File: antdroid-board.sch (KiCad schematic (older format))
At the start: 7 parts

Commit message: Added Servo Power Supply
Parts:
- added C? (x2): 200µF, symbol C
- added C? (x2): 0.01µF, symbol C
- added C? (x2): 500µF, symbol C
- added D?: 1N5822, DO-204AL, symbol 1N5822
- added D?: MBR745, TO-220, symbol MBR745
- added IC?: LT1076CT, linear-technology-2-TO220-5, symbol LT1076CT
- added IC?: LT1074CT, linear-technology-2-TO220-5, symbol LT1074CT
- added L?: 100µH, symbol INDUCTOR
- added L?: 50µH, symbol INDUCTOR
- added R? (x2): 2.7k, symbol R
- added R? (x2): 2.8k, symbol R
- added R? (x2): 2.21k, symbol R
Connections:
- net labels added: GND, VCC
- wire segments 16 -> 42
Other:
- note added: "RPI POWER SUPPLY"
- note added: "SERIAL RPI"
- note added: "SERVOS POWER SUPPLY"
- note removed: "SERIAL_RPI"
- moved on the sheet: SHIELD?

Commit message: Change power supply to LM26XX
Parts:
- removed C? (x2): 200µF, symbol C
- removed C? (x2): 0.01µF, symbol C
- removed C? (x2): 500µF, symbol C
- removed D?: 1N5822, DO-204AL, symbol 1N5822
- removed D?: MBR745, TO-220, symbol MBR745
- removed IC?: LT1076CT, linear-technology-2-TO220-5, symbol LT1076CT
- removed IC?: LT1074CT, linear-technology-2-TO220-5, symbol LT1074CT
- removed L?: 100µH, symbol INDUCTOR
- removed L?: 50µH, symbol INDUCTOR
- removed R? (x2): 10K, symbol R
- removed R? (x2): 2.7k, symbol R
- removed R? (x2): 2.8k, symbol R
- removed R? (x2): 2.21k, symbol R
- added C? (x6): 15µF/50V, symbol CP
- added C? (x2): 0,01µF, symbol C
- added C? (x2): 0.47µF, symbol C
- added C? (x4): 180µF/16V, symbol CP
- added C?: C, symbol C
- added C?: 10nF, symbol C
- added C?: 68µF, symbol C
- added D? (x2): MBR745G, DO-204AL, symbol MBR745G
- added D?: 1N5822, DO-204AL, symbol 1N5822
- added L? (x2): 22µH, symbol INDUCTOR
- added L?: 47µH, symbol INDUCTOR
- added R? (x2): 10K, symbol R
- added U? (x2): LM2678T-5.0, TO-220, symbol LM2678T-5.0
- added U?: LM2675M-5, SOIC-8, symbol LM2675M-5
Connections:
- net labels added: +5VA
- wire segments 42 -> 54
- no-connect marks 0 -> 1
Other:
- note added: "SERVO POWER LED"
- moved on the sheet: Q?, R?, SHIELD?

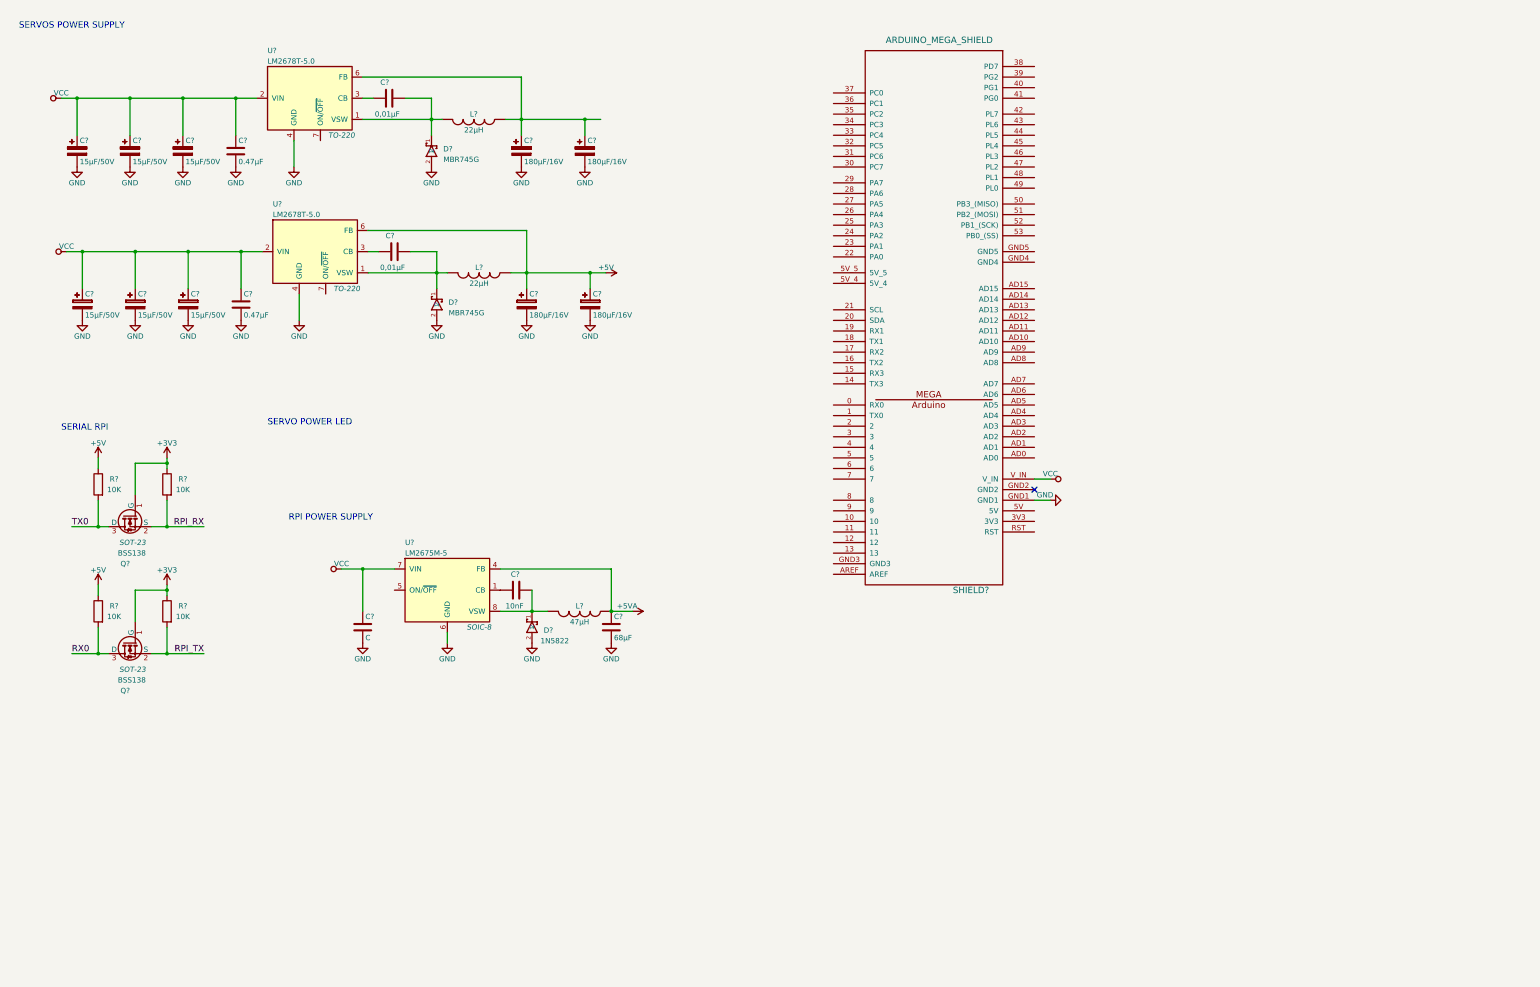
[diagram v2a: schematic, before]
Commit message: Added JP of servos
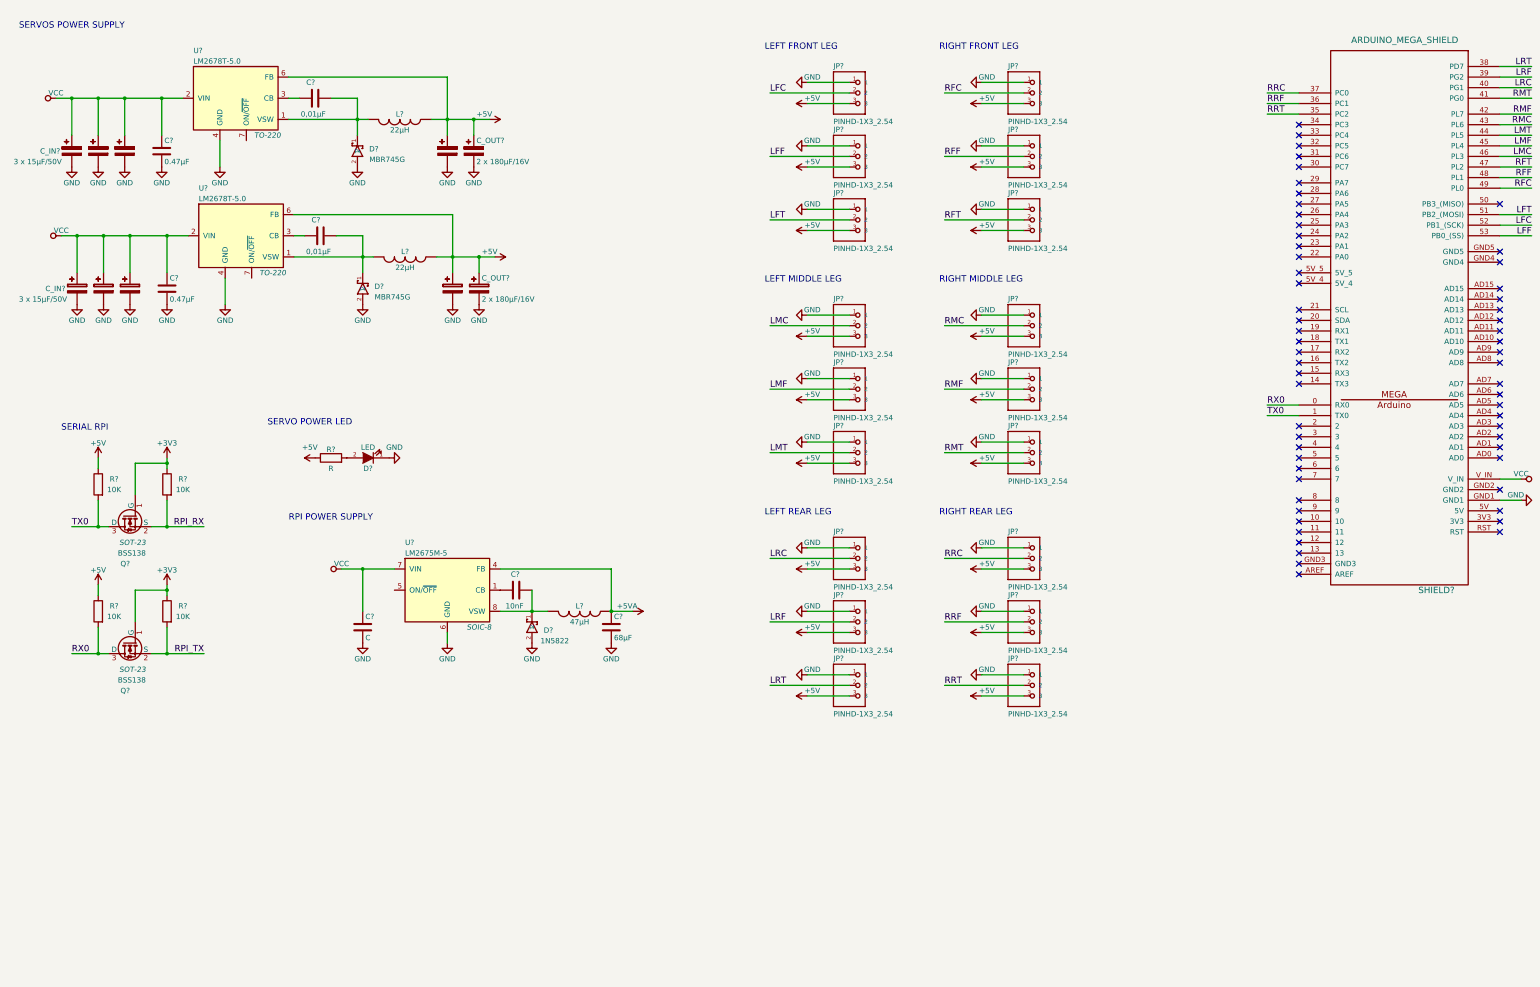
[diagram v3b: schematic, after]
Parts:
- removed C? (x3): 15µF/50V, symbol CP
- removed C?: 0.47µF, symbol C
- removed C?: 0,01µF, symbol C
- removed C? (x2): 180µF/16V, symbol CP
- removed D?: MBR745G, DO-204AL, symbol MBR745G
- removed L?: 22µH, symbol INDUCTOR
- removed U?: LM2678T-5.0, TO-220, symbol LM2678T-5.0
- added C? (x2): 15µF/50V, symbol CP
- added C?: 0.47µF, symbol C
- added C?: 0,01µF, symbol C
- added C?: 180µF/16V, symbol CP
- added C_IN?: 3 x 15µF/50V, symbol CP
- added C_OUT?: 2 x 180µF/16V, symbol CP
- added D?: MBR745G, DO-204AL, symbol MBR745G
- added D?: LED, symbol LED
- added JP? (x18): PINHD-1X3_2.54, pinhead-1-1X03, symbol PINHD-1X3_2.54
- added L?: 22µH, symbol INDUCTOR
- added R?: R, symbol R
- added U?: LM2678T-5.0, TO-220, symbol LM2678T-5.0
- C_IN?: renamed from C?; value 15µF/50V -> 3 x 15µF/50V
- C_OUT?: renamed from C?; value 180µF/16V -> 2 x 180µF/16V
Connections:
- net +5V: now also C?.1, C_OUT?.1, L?.1, U?.6 (FB), C?.1, C_OUT?.1, JP?.3, JP?.3, JP?.3, JP?.3, JP?.3, JP?.3, JP?.3, JP?.3, JP?.3, JP?.3, JP?.3, JP?.3, JP?.3, JP?.3, JP?.3, JP?.3, JP?.3, JP?.3, L?.1, R?.1, U?.6 (FB)
- net GND: now also C?.2, C?.2, C?.2, C?.2, C_IN?.2, C_OUT?.2, D?.1 (K), D?.2, JP?.1, JP?.1, JP?.1, JP?.1, JP?.1, JP?.1, JP?.1, JP?.1, JP?.1, JP?.1, JP?.1, JP?.1, JP?.1, JP?.1, JP?.1, JP?.1, JP?.1, JP?.1, U?.4 (GND)
- net RX0: now also SHIELD?.0 (RX0)
- net TX0: now also SHIELD?.1 (TX0)
- net VCC: now also C?.1, C?.1, C?.1, C_IN?.1, U?.2 (VIN)
- net RRT: now reaches SHIELD?.35 (PC2)
- net RRT: now also JP?.2
- net RRF: now reaches SHIELD?.36 (PC1)
- net RRF: now also JP?.2
- net RRC: now reaches SHIELD?.37 (PC0)
- net RRC: now also JP?.2
- net LRT: now reaches SHIELD?.38 (PD7)
- net LRT: now also JP?.2
- net LRF: now reaches SHIELD?.39 (PG2)
- net LRF: now also JP?.2
- net LRC: now reaches SHIELD?.40 (PG1)
- net LRC: now also JP?.2
- net RMT: now reaches SHIELD?.41 (PG0)
- net RMT: now also JP?.2
- net RMF: now reaches SHIELD?.42 (PL7)
- net RMF: now also JP?.2
- net RMC: now reaches SHIELD?.43 (PL6)
- net RMC: now also JP?.2
- net LMT: now reaches SHIELD?.44 (PL5)
- net LMT: now also JP?.2
- net LMF: now reaches SHIELD?.45 (PL4)
- net LMF: now also JP?.2
- net LMC: now reaches SHIELD?.46 (PL3)
- net LMC: now also JP?.2
- net RFT: now reaches SHIELD?.47 (PL2)
- net RFT: now also JP?.2
- net RFF: now reaches SHIELD?.48 (PL1)
- net RFF: now also JP?.2
- net RFC: now reaches SHIELD?.49 (PL0)
- net RFC: now also JP?.2
- net LFT: now reaches SHIELD?.51 (PB2_(MOSI))
- net LFT: now also JP?.2
- net LFC: now reaches SHIELD?.52 (PB1_(SCK))
- net LFC: now also JP?.2
- net LFF: now reaches SHIELD?.53 (PB0_(SS))
- net LFF: now also JP?.2
- new net: C?.2, D?.1, L?.2, U?.1 (VSW)
- new net: C?.1, U?.3 (CB)
- new net: D?.2 (A), R?.2
- no-connect marks 1 -> 60
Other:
- note added: "LEFT FRONT LEG"
- note added: "LEFT MIDDLE LEG"
- note added: "LEFT REAR LEG"
- note added: "RIGHT FRONT LEG"
- note added: "RIGHT MIDDLE LEG"
- note added: "RIGHT REAR LEG"
- moved on the sheet: C?, C_IN?, C_OUT?, D?, L?, SHIELD?, U?

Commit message: Added PWR_FLAGS
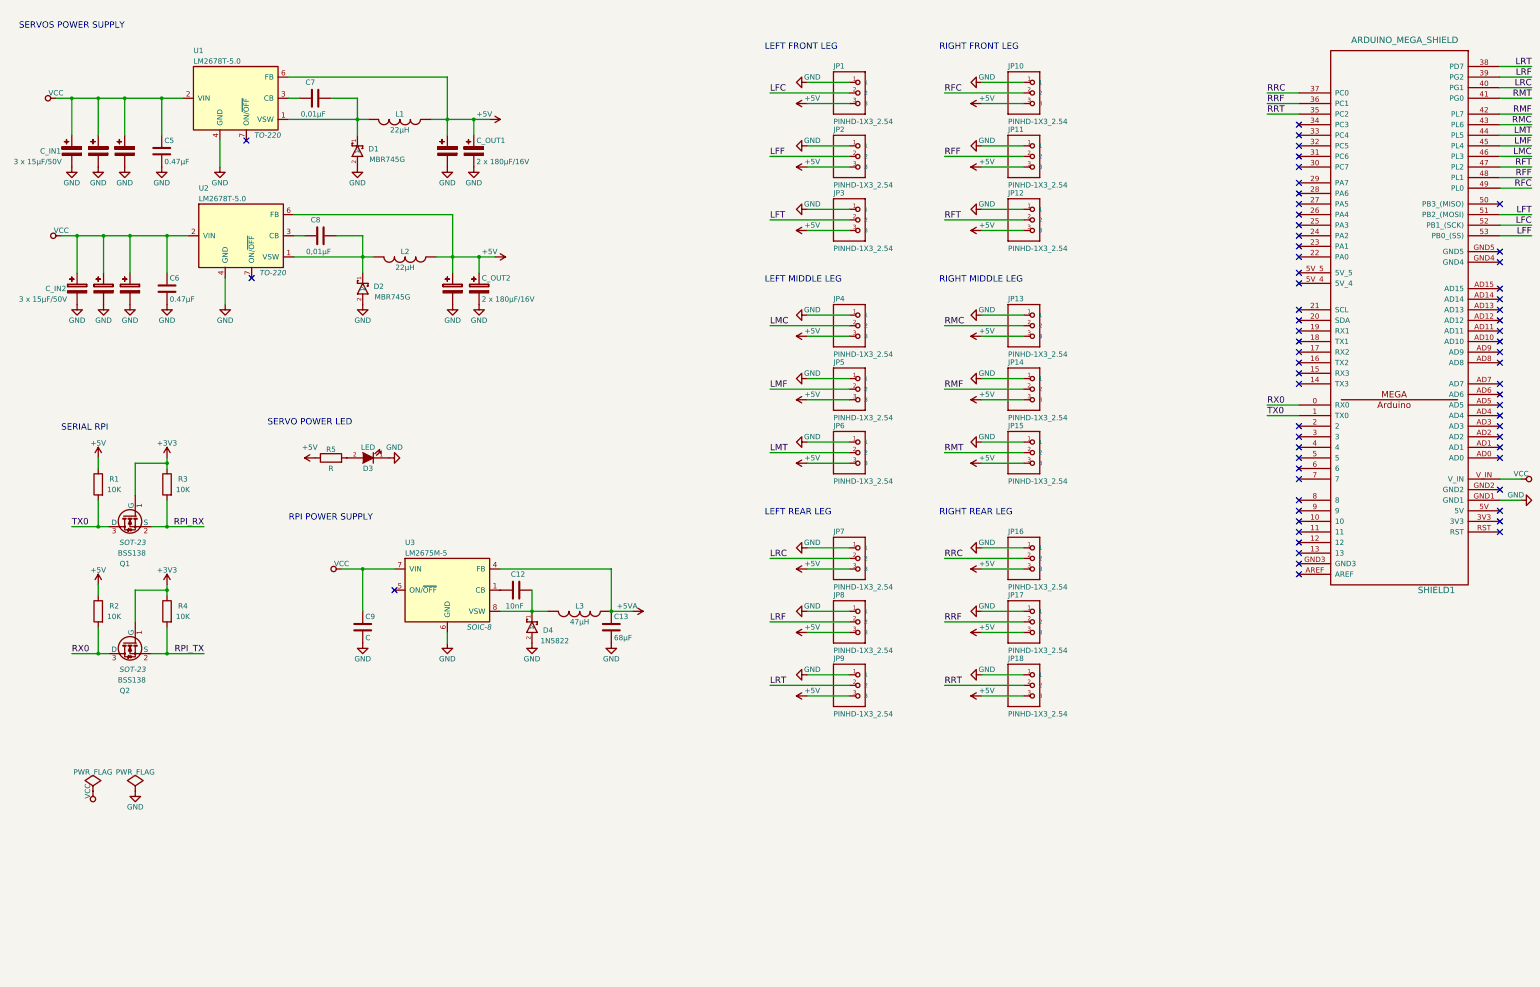
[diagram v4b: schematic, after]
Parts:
- gave numbers to parts that had none: 53
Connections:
- no-connect marks 60 -> 63
